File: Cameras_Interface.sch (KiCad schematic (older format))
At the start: 18 parts, among them J9 WE_68715014522, U9 MAX13042EEBC+T

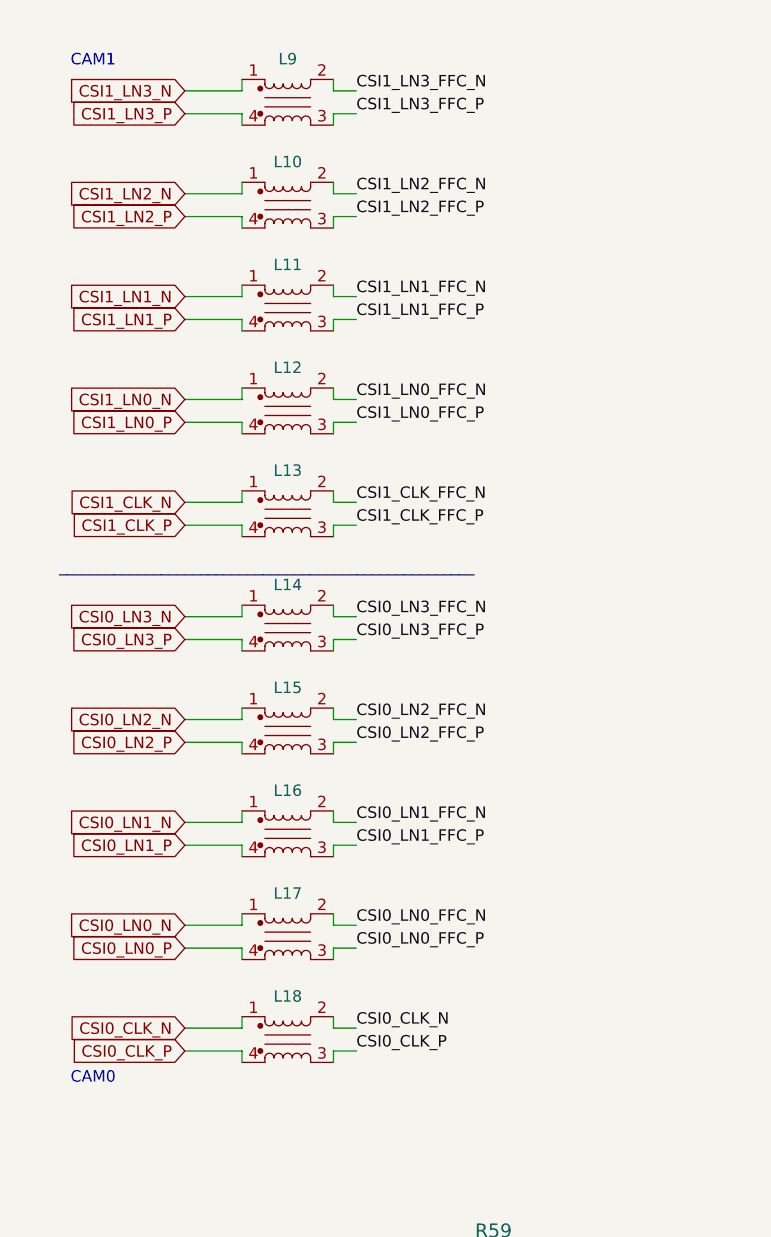
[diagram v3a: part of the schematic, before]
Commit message: replaced common mode chokes, dedicated for hdmi and with smaller footprint
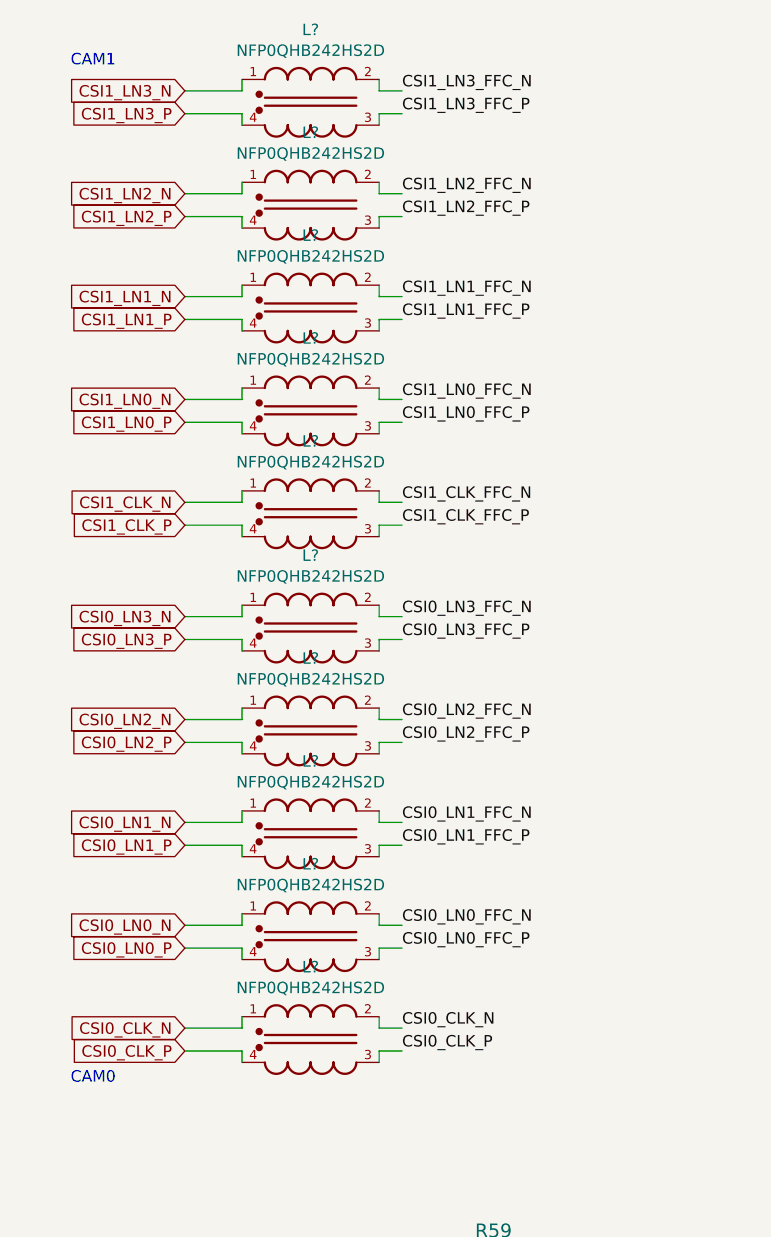
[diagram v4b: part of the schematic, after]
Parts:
- removed L10, L11, L12, L13, L14, L15, L16, L17, L18, L9: 744235900, antmicro-footprints:744235900, symbol antmicroFixedInductors:744235900
- added L? (x10): NFP0QHB242HS2D, antmicro-footprints:FIL_NFP0QHB242HS2D, symbol antmicroFixedInductors:NFP0QHB242HS2D
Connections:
- net CSI0_CLK_N: now also L?.1, L?.2
- net CSI0_CLK_P: now also L?.3, L?.4
- net CSI0_LN0_FFC_N: now also L?.2
- net CSI0_LN0_FFC_P: now also L?.3
- net CSI0_LN0_N: now also L?.1
- net CSI0_LN0_P: now also L?.4
- net CSI0_LN1_FFC_N: now also L?.2
- net CSI0_LN1_FFC_P: now also L?.3
- net CSI0_LN1_N: now also L?.1
- net CSI0_LN1_P: now also L?.4
- net CSI0_LN2_FFC_N: now also L?.2
- net CSI0_LN2_FFC_P: now also L?.3
- net CSI0_LN2_N: now also L?.1
- net CSI0_LN2_P: now also L?.4
- net CSI0_LN3_FFC_N: now also L?.2
- net CSI0_LN3_FFC_P: now also L?.3
- net CSI0_LN3_N: now also L?.1
- net CSI0_LN3_P: now also L?.4
- net CSI1_CLK_FFC_N: now also L?.2
- net CSI1_CLK_FFC_P: now also L?.3
- net CSI1_CLK_N: now also L?.1
- net CSI1_CLK_P: now also L?.4
- net CSI1_LN0_FFC_N: now also L?.2
- net CSI1_LN0_FFC_P: now also L?.3
- net CSI1_LN0_N: now also L?.1
- net CSI1_LN0_P: now also L?.4
- net CSI1_LN1_FFC_N: now also L?.2
- net CSI1_LN1_FFC_P: now also L?.3
- net CSI1_LN1_N: now also L?.1
- net CSI1_LN1_P: now also L?.4
- net CSI1_LN2_FFC_N: now also L?.2
- net CSI1_LN2_FFC_P: now also L?.3
- net CSI1_LN2_N: now also L?.1
- net CSI1_LN2_P: now also L?.4
- net CSI1_LN3_FFC_N: now also L?.2
- net CSI1_LN3_FFC_P: now also L?.3
- net CSI1_LN3_N: now also L?.1
- net CSI1_LN3_P: now also L?.4
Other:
- note removed: "_____________________________________________________\n\n"

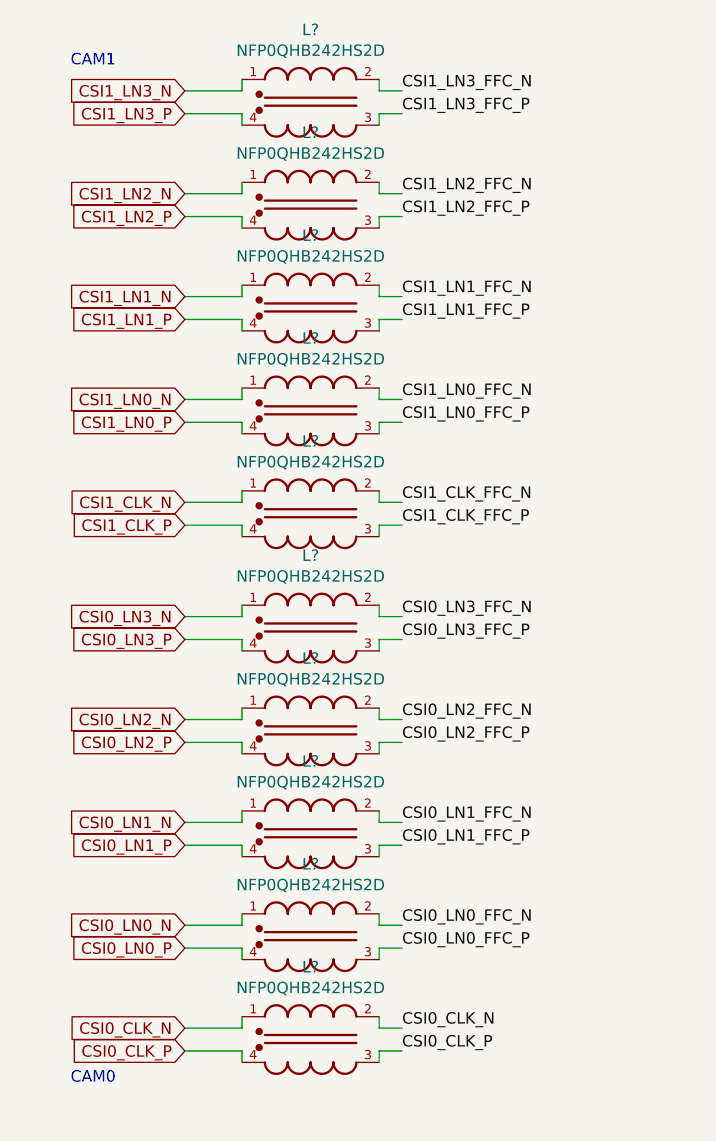
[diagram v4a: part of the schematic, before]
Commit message: modified layout of the board so that ethernet is further away from poe psu
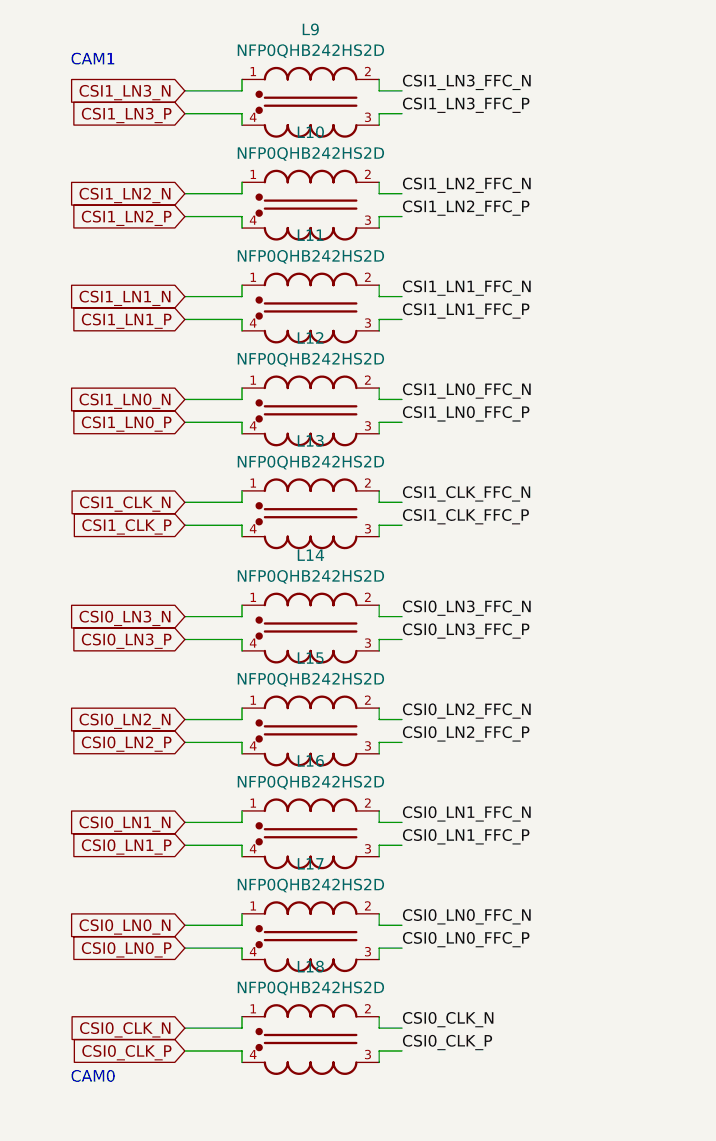
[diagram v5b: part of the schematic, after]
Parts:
- gave numbers to parts that had none: 10
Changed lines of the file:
@@
 	7450 6550 7450 6750
 $Comp
-L antmicroFixedInductors:NFP0QHB242HS2D L?
+L antmicroFixedInductors:NFP0QHB242HS2D L9
 U 1 1 61CE378A
 P 1750 1600
-F 0 "L?" H 1750 1917 50  0000 C CNN
+F 0 "L9" H 1750 1917 50  0000 C CNN
 F 1 "NFP0QHB242HS2D" H 1750 1826 50  0000 C CNN
 F 2 "antmicro-footprints:FIL_NFP0QHB242HS2D" H 1505 1930 50  0001 C CNN
@@
 $EndComp
 $Comp
-L antmicroFixedInductors:NFP0QHB242HS2D L?
+L antmicroFixedInductors:NFP0QHB242HS2D L10
 U 1 1 61CECE67
 P 1750 2050
-F 0 "L?" H 1750 2367 50  0000 C CNN
+F 0 "L10" H 1750 2367 50  0000 C CNN
 F 1 "NFP0QHB242HS2D" H 1750 2276 50  0000 C CNN
 F 2 "antmicro-footprints:FIL_NFP0QHB242HS2D" H 1505 2380 50  0001 C CNN
@@
 $EndComp
 $Comp
-L antmicroFixedInductors:NFP0QHB242HS2D L?
+L antmicroFixedInductors:NFP0QHB242HS2D L11
 U 1 1 61CED3A2
 P 1750 2500
-F 0 "L?" H 1750 2817 50  0000 C CNN
+F 0 "L11" H 1750 2817 50  0000 C CNN
 F 1 "NFP0QHB242HS2D" H 1750 2726 50  0000 C CNN
 F 2 "antmicro-footprints:FIL_NFP0QHB242HS2D" H 1505 2830 50  0001 C CNN
@@
 $EndComp
 $Comp
-L antmicroFixedInductors:NFP0QHB242HS2D L?
+L antmicroFixedInductors:NFP0QHB242HS2D L12
 U 1 1 61CEDD0B
 P 1750 2950
-F 0 "L?" H 1750 3267 50  0000 C CNN
+F 0 "L12" H 1750 3267 50  0000 C CNN
 F 1 "NFP0QHB242HS2D" H 1750 3176 50  0000 C CNN
 F 2 "antmicro-footprints:FIL_NFP0QHB242HS2D" H 1505 3280 50  0001 C CNN
@@
 $EndComp
 $Comp
-L antmicroFixedInductors:NFP0QHB242HS2D L?
+L antmicroFixedInductors:NFP0QHB242HS2D L13
 U 1 1 61CEE413
 P 1750 3400
-F 0 "L?" H 1750 3717 50  0000 C CNN
+F 0 "L13" H 1750 3717 50  0000 C CNN
 F 1 "NFP0QHB242HS2D" H 1750 3626 50  0000 C CNN
 F 2 "antmicro-footprints:FIL_NFP0QHB242HS2D" H 1505 3730 50  0001 C CNN
@@
 $EndComp
 $Comp
-L antmicroFixedInductors:NFP0QHB242HS2D L?
+L antmicroFixedInductors:NFP0QHB242HS2D L14
 U 1 1 61CEE814
 P 1750 3900
-F 0 "L?" H 1750 4217 50  0000 C CNN
+F 0 "L14" H 1750 4217 50  0000 C CNN
 F 1 "NFP0QHB242HS2D" H 1750 4126 50  0000 C CNN
 F 2 "antmicro-footprints:FIL_NFP0QHB242HS2D" H 1505 4230 50  0001 C CNN
@@
 $EndComp
 $Comp
-L antmicroFixedInductors:NFP0QHB242HS2D L?
+L antmicroFixedInductors:NFP0QHB242HS2D L15
 U 1 1 61CEEFBB
 P 1750 4350
-F 0 "L?" H 1750 4667 50  0000 C CNN
+F 0 "L15" H 1750 4667 50  0000 C CNN
 F 1 "NFP0QHB242HS2D" H 1750 4576 50  0000 C CNN
 F 2 "antmicro-footprints:FIL_NFP0QHB242HS2D" H 1505 4680 50  0001 C CNN
@@
 $EndComp
 $Comp
-L antmicroFixedInductors:NFP0QHB242HS2D L?
+L antmicroFixedInductors:NFP0QHB242HS2D L16
 U 1 1 61CEFBB4
 P 1750 4800
-F 0 "L?" H 1750 5117 50  0000 C CNN
+F 0 "L16" H 1750 5117 50  0000 C CNN
 F 1 "NFP0QHB242HS2D" H 1750 5026 50  0000 C CNN
 F 2 "antmicro-footprints:FIL_NFP0QHB242HS2D" H 1505 5130 50  0001 C CNN
@@
 $EndComp
 $Comp
-L antmicroFixedInductors:NFP0QHB242HS2D L?
+L antmicroFixedInductors:NFP0QHB242HS2D L17
 U 1 1 61CF063F
 P 1750 5250
-F 0 "L?" H 1750 5567 50  0000 C CNN
+F 0 "L17" H 1750 5567 50  0000 C CNN
 F 1 "NFP0QHB242HS2D" H 1750 5476 50  0000 C CNN
 F 2 "antmicro-footprints:FIL_NFP0QHB242HS2D" H 1505 5580 50  0001 C CNN
@@
 $EndComp
 $Comp
-L antmicroFixedInductors:NFP0QHB242HS2D L?
+L antmicroFixedInductors:NFP0QHB242HS2D L18
 U 1 1 61CF0B6C
 P 1750 5700
-F 0 "L?" H 1750 6017 50  0000 C CNN
+F 0 "L18" H 1750 6017 50  0000 C CNN
 F 1 "NFP0QHB242HS2D" H 1750 5926 50  0000 C CNN
 F 2 "antmicro-footprints:FIL_NFP0QHB242HS2D" H 1505 6030 50  0001 C CNN
